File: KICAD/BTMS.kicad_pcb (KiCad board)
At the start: 4 copper layers, 76.2 x 55.1 mm, 151 parts, among them J1 Batt_Ballance, J2 AUX_Charge, J3 Battery_IO, J4 Power_Out, J5 BT_LM62, J6 DSKY, J7 PWR_SW, J8 ICSP, J9 Heater, P1 USB_C_Plug, Q1 SSM3K341R, Q2 DMN65D8L, Q3 SSM3K341R, Q4 FDN340P, Q5 FDN340P, Q6 FDN340P, Q7 DMN65D8L, Q8 DMN65D8L, U1 ACS711xLCTR-25AB, U10 BA033CC0FP-E2, U11 AON7522E, U12 AON7522E, U13 LM62CIM3/NOPB, U14 FAN3100TSX, U15 FAN3100TSX, U16 AON7522E, U17 dsPIC30F3011-PT, U18 FT230XQ, U2 AP33771, U3 IS281-4, U4 Q294700DSGR, U5 SCF4030-12-0X, U6 AONR21321, U7 ACS711xLCTR-25AB, U8 IS281-4, U9 IRS2184

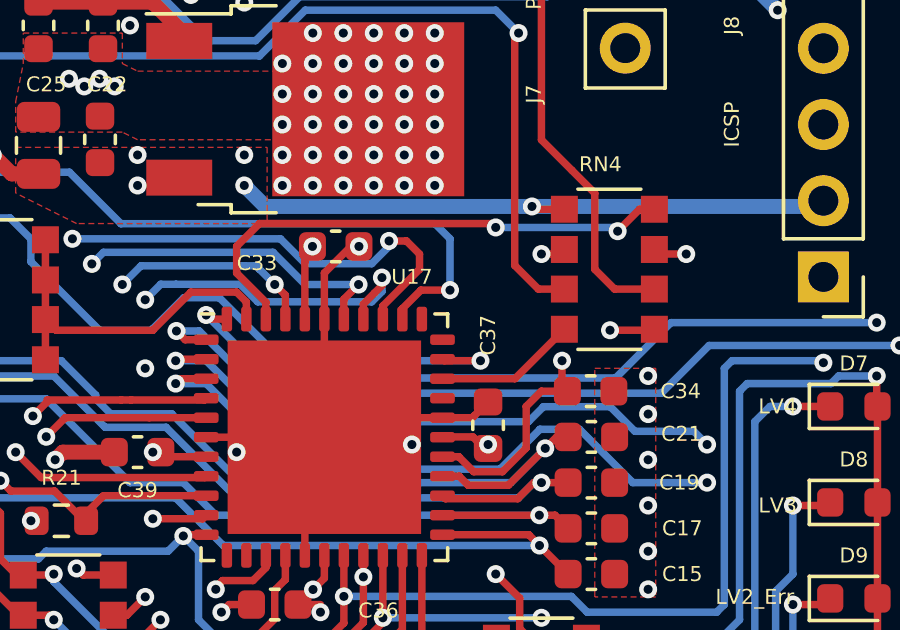
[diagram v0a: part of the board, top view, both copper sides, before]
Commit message: Cleaned up ground plane islands.
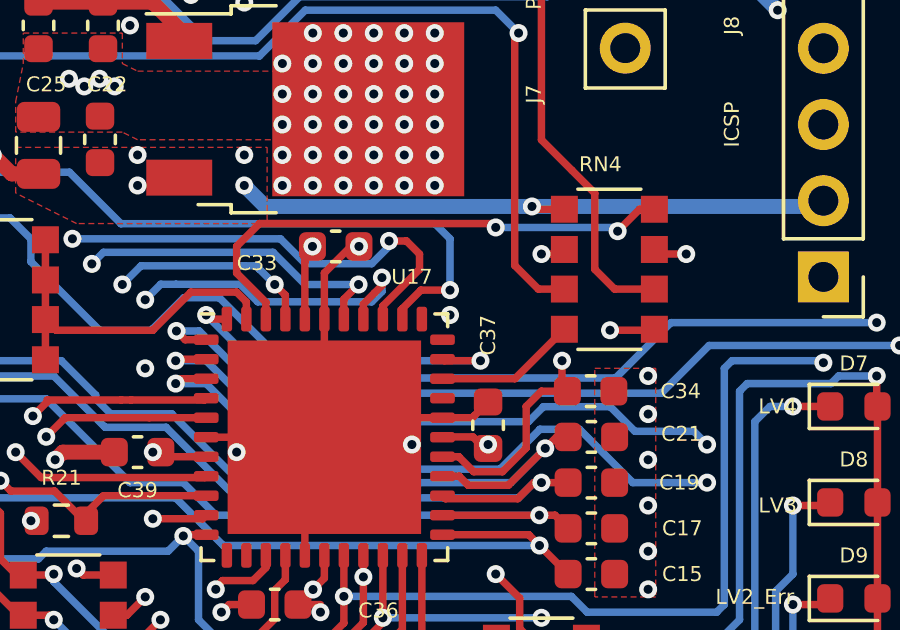
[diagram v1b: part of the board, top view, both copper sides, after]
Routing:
- net GND: vias 168 -> 169
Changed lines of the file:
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@@
   (via (at 169.418 103.886) (size 0.6) (drill 0.3) (layers "F.Cu" "B.Cu") (net 6))
   (via (at 183.388 96.52) (size 0.6) (drill 0.3) (layers "F.Cu" "B.Cu") (free) (net 6))
+  (via (at 171.958 112.268) (size 0.6) (drill 0.3) (layers "F.Cu" "B.Cu") (free) (net 6))
   (via (at 178.562 120.142) (size 0.6) (drill 0.3) (layers "F.Cu" "B.Cu") (free) (net 6))
   (via (at 170.434 103.886) (size 0.6) (drill 0.3) (layers "F.Cu" "B.Cu") (net 6))
@@
     )
   )
+  (zone (net 0) (net_name "") (layer "B.Cu") (hatch edge 0.508)
+    (connect_pads yes (clearance 0))
+    (min_thickness 0.254)
+    (keepout (tracks allowed) (vias allowed) (pads allowed) (copperpour not_allowed) (footprints allowed))
+    (fill (thermal_gap 0.508) (thermal_bridge_width 0.508))
+    (polygon
+      (pts
+        (xy 177.8 118.364)
+        (xy 180.848 118.364)
+        (xy 180.848 121.666)
+        (xy 176.784 121.666)
+        (xy 175.514 120.904)
+        (xy 175.514 116.332)
+        (xy 176.276 116.332)
+      )
+    )
+  )
   (zone (net 6) (net_name "GND") (layer "B.Cu") (hatch edge 0.508)
     (connect_pads yes (clearance 0.2))
@@
     (polygon
       (pts
+        (xy 175.006 101.854)
+        (xy 166.878 101.6)
+        (xy 167.64 102.616)
+        (xy 163.576 102.616)
+        (xy 163.576 99.807059)
+        (xy 162.814 99.06)
+        (xy 146.05 98.806)
+        (xy 146.05 98.298)
+        (xy 163.068 98.298)
+        (xy 165.354 100.584)
+        (xy 175.006 100.584)
+      )
+    )
+  )
+  (zone (net 0) (net_name "") (layer "B.Cu") (hatch edge 0.508)
+    (connect_pads yes (clearance 0))
+    (min_thickness 0.254)
+    (keepout (tracks allowed) (vias allowed) (pads allowed) (copperpour not_allowed) (footprints allowed))
+    (fill (thermal_gap 0.508) (thermal_bridge_width 0.508))
+    (polygon
+      (pts
         (xy 183.134 118.872)
         (xy 182.372 118.872)
@@
     (polygon
       (pts
-        (xy 169.672 113.538)
-        (xy 169.164 113.538)
-        (xy 169.164 112.268)
-        (xy 169.672 112.014)
+        (xy 171.45 113.538)
+        (xy 166.116 113.538)
+        (xy 166.116 111.506)
+        (xy 171.45 111.506)
+      )
+    )
+  )
+  (zone (net 0) (net_name "") (layer "B.Cu") (hatch edge 0.508)
+    (connect_pads yes (clearance 0))
+    (min_thickness 0.254)
+    (keepout (tracks allowed) (vias allowed) (pads allowed) (copperpour not_allowed) (footprints allowed))
+    (fill (thermal_gap 0.508) (thermal_bridge_width 0.508))
+    (polygon
+      (pts
+        (xy 169.672 110.49)
+        (xy 167.386 110.49)
+        (xy 167.386 109.22)
+        (xy 169.672 109.22)
+      )
+    )
+  )
+  (zone (net 0) (net_name "") (layer "B.Cu") (hatch edge 0.508)
+    (connect_pads yes (clearance 0))
+    (min_thickness 0.254)
+    (keepout (tracks allowed) (vias allowed) (pads allowed) (copperpour not_allowed) (footprints allowed))
+    (fill (thermal_gap 0.508) (thermal_bridge_width 0.508))
+    (polygon
+      (pts
+        (xy 160.782 109.474)
+        (xy 161.798 112.522)
+        (xy 160.528 112.776)
+        (xy 158.242 110.49)
+        (xy 157.734 108.966)
+        (xy 151.13 108.966)
+        (xy 151.13 107.696)
+        (xy 159.004 107.696)
       )
     )
@@
     )
   )
+  (zone (net 0) (net_name "") (layer "B.Cu") (hatch edge 0.508)
+    (connect_pads yes (clearance 0))
+    (min_thickness 0.254)
+    (keepout (tracks allowed) (vias allowed) (pads allowed) (copperpour not_allowed) (footprints allowed))
+    (fill (thermal_gap 0.508) (thermal_bridge_width 0.508))
+    (polygon
+      (pts
+        (xy 143.256 137.16)
+        (xy 143.256 141.732)
+        (xy 142.24 141.732)
+        (xy 142.24 137.668)
+        (xy 140.208 135.636)
+        (xy 140.97 135.636)
+      )
+    )
+  )
   (zone (net 6) (net_name "GND") (layer "B.Cu") (hatch edge 0.508)
     (connect_pads yes (clearance 0.2))
@@
     (polygon
       (pts
+        (xy 125.73 133.35)
+        (xy 123.19 133.35)
+        (xy 121.158 134.874)
+        (xy 120.65 134.62)
+        (xy 122.682 132.842)
+        (xy 125.73 132.842)
+      )
+    )
+  )
+  (zone (net 0) (net_name "") (layer "B.Cu") (hatch edge 0.508)
+    (connect_pads yes (clearance 0))
+    (min_thickness 0.254)
+    (keepout (tracks allowed) (vias allowed) (pads allowed) (copperpour not_allowed) (footprints allowed))
+    (fill (thermal_gap 0.508) (thermal_bridge_width 0.508))
+    (polygon
+      (pts
         (xy 141.732 141.732)
         (xy 141.224 141.732)
@@
       )
     )
+  )
+  (zone (net 0) (net_name "") (layer "B.Cu") (hatch edge 0.508)
+    (connect_pads yes (clearance 0))
+    (min_thickness 0.254)
+    (keepout (tracks allowed) (vias allowed) (pads allowed) (copperpour not_allowed) (footprints allowed))
+    (fill (thermal_gap 0.508) (thermal_bridge_width 0.508))
+    (polygon
+      (pts
+        (xy 180.848 117.856)
+        (xy 177.8 117.602)
+        (xy 176.022 115.824)
+        (xy 179.07 113.03)
+        (xy 180.848 113.03)
+      )
+    )
+  )
+  (zone (net 0) (net_name "") (layer "B.Cu") (hatch edge 0.508)
+    (connect_pads yes (clearance 0))
+    (min_thickness 0.254)
+    (keepout (tracks allowed) (vias allowed) (pads allowed) (copperpour not_allowed) (footprints allowed))
+    (fill (thermal_gap 0.508) (thermal_bridge_width 0.508))
+    (polygon
+      (pts
+        (xy 157.734 110.744)
+        (xy 156.972 110.744)
+        (xy 156.972 110.236)
+        (xy 157.734 110.236)
+      )
+    )

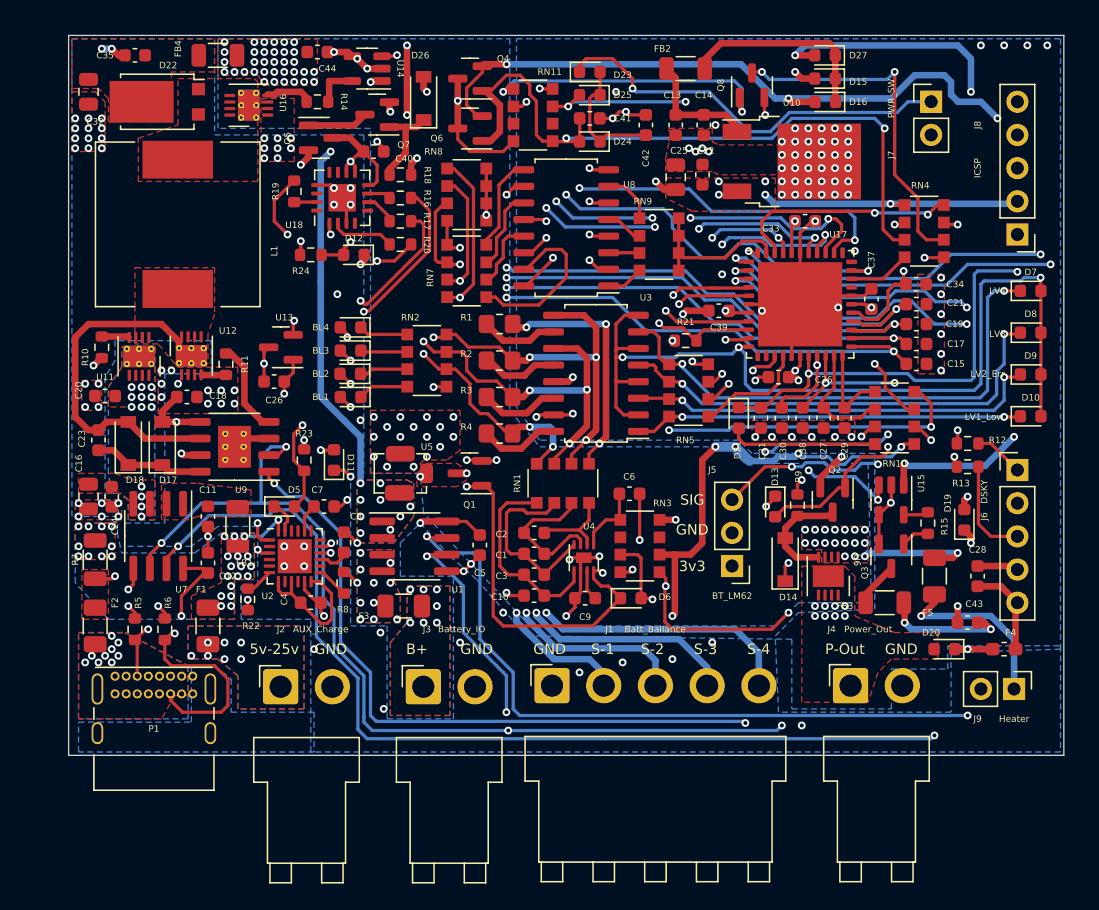
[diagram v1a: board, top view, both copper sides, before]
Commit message: Extended board and placed mounting points.
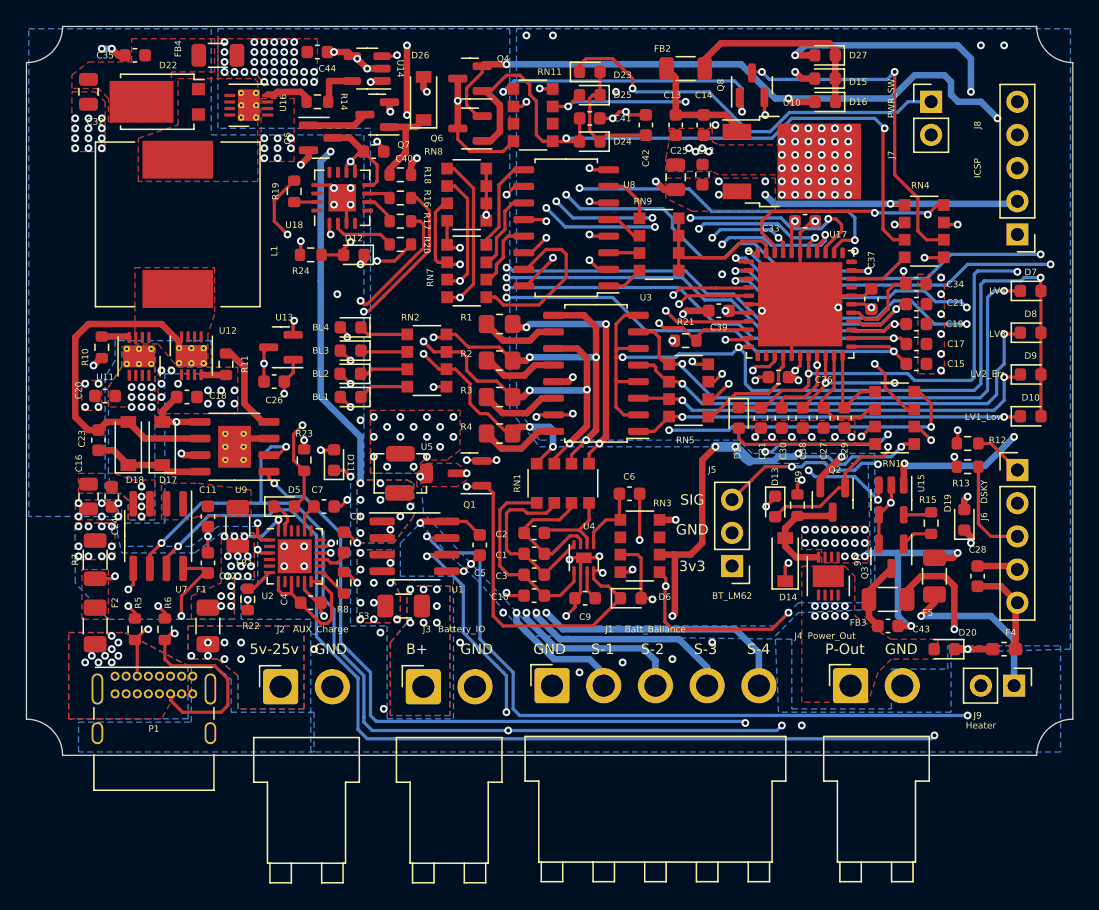
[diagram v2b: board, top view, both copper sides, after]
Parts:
- R15: value 12 -> 27R
- moved C43 6.10 mm to (174.5, 141.0), turned to 180 degrees
- moved FB3 0.36 mm to (174.5, 138.9)
- moved R15 0.25 mm to (177.8, 133.1), turned to -90 degrees
- moved J9 0.25 mm to (184.2, 145.5)
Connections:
- C43 pad 2: Net-(C43-Pad2) -> Net-(Q3-Pad3)
- FB3 pad 1: Net-(FB3-Pad1) -> Net-(Q3-Pad3)
- FB3 pad 2: Net-(C43-Pad2) -> Net-(J9-Pad2)
- J9 pad 2: Net-(C43-Pad2) -> Net-(J9-Pad2)
- Q3 pad 3: Net-(FB3-Pad1) -> Net-(Q3-Pad3)
- R15 pad 1: Net-(Q3-Pad1) -> Net-(U15-Pad5)
- R15 pad 2: Net-(R15-Pad2) -> Net-(Q3-Pad1)
- U15 pad 5: Net-(R15-Pad2) -> Net-(U15-Pad5)
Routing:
- net Net-(C43-Pad2): track 14.5 -> 0.00 mm, vias 2 -> 0
- net Net-(J9-Pad2): track 0.00 -> 14.3 mm, vias 0 -> 1
- net Net-(Q3-Pad3): track 0.00 -> 5.39 mm
- net Net-(FB3-Pad1): track 3.43 -> 0.00 mm
- net Net-(U15-Pad5): track 0.00 -> 1.92 mm
- net Net-(R15-Pad2): track 1.92 -> 0.00 mm
- net /ExtBus: track 17.2 -> 19.1 mm
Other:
- board size 76.2 x 55.1 mm -> 80.1 x 55.8 mm
